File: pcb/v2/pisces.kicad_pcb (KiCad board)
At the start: 2 copper layers, 137.8 x 60.1 mm, 61 parts, among them J1 USB_B_Micro, J2 AudioJack4, SW1 SW_PUSH, SW10 SW_PUSH, SW11 SW_PUSH, SW12 SW_PUSH, SW13 SW_PUSH, SW14 SW_PUSH, SW15 SW_PUSH, SW16 SW_PUSH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

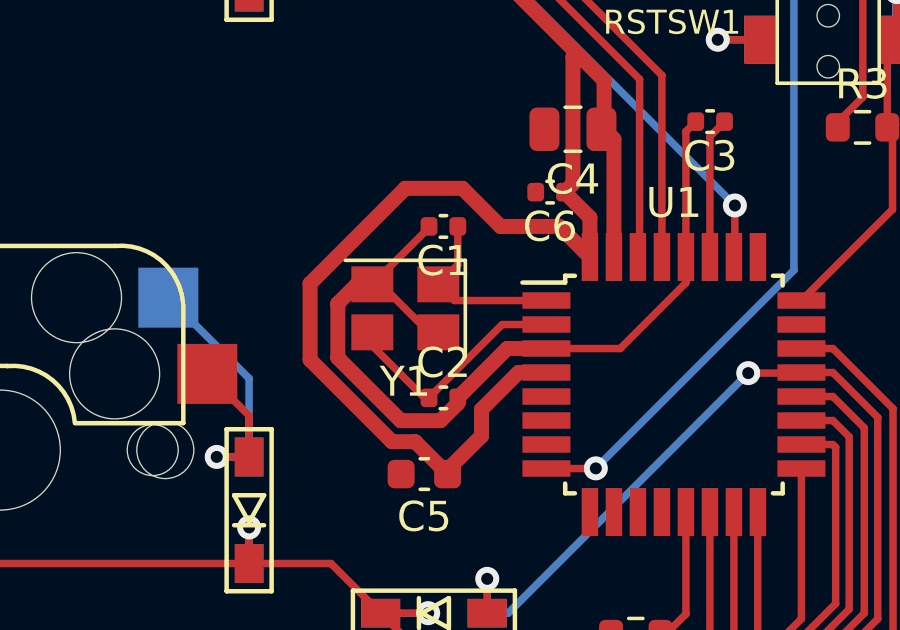
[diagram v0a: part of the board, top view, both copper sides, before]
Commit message: Removed external link to footprint library (#33)
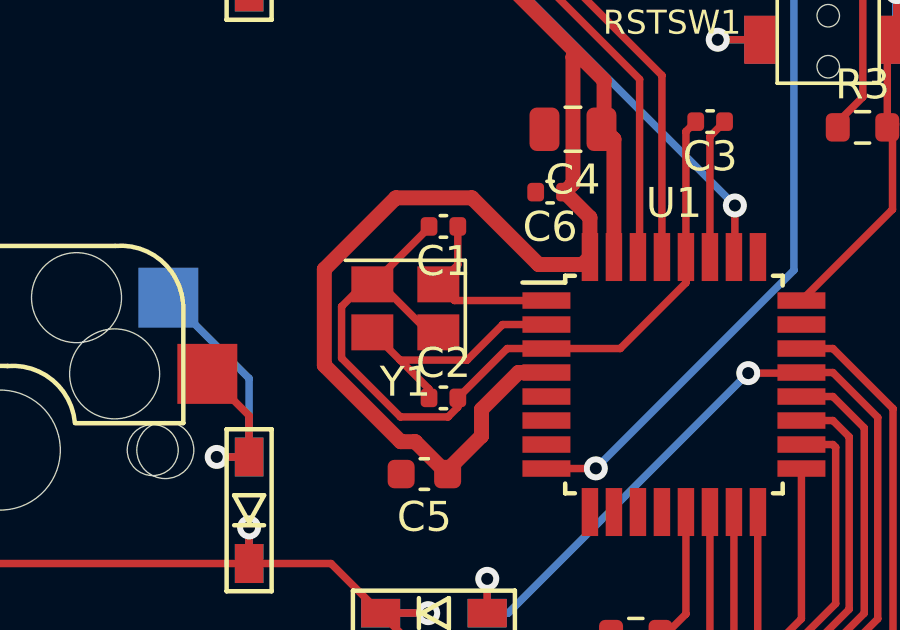
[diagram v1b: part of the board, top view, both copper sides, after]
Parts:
- D1, D10, D11, D12, D13, D14, D15, D16, D17, D18, D19, D2, D3, D4, D5, D6, D7, D8, D9, D_H1: footprint kbd:D3_SMD -> pisces_v2:D3_SMD
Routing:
- net VCC: track 75.2 -> 74.6 mm

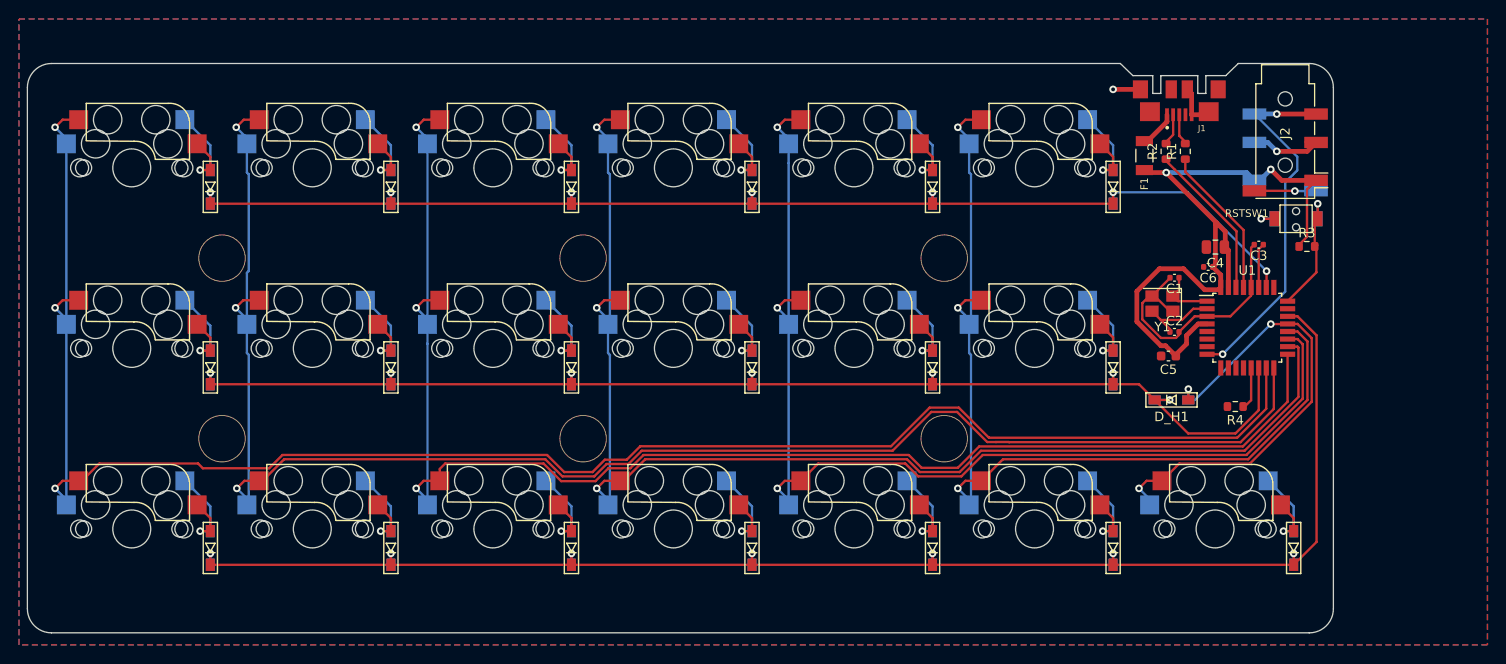
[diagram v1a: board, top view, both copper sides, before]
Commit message: KiCad Updated to 6.0.7 (#34)
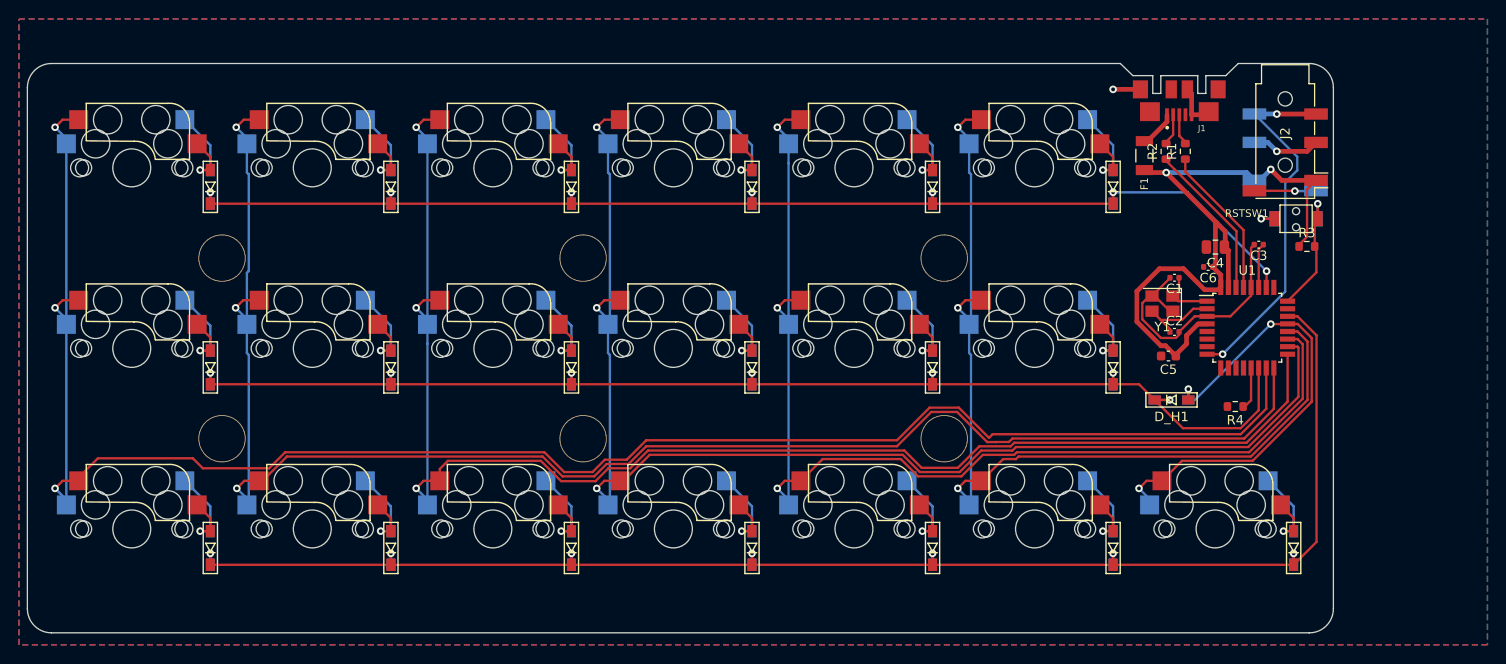
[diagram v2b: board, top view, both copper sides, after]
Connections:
- J1 pad 4: Net-(J1-Pad4) -> unconnected-(J1-Pad4)
- J2 pad S: Net-(J2-PadS) -> unconnected-(J2-PadS)
- U1 pad 10: Net-(U1-Pad10) -> unconnected-(U1-Pad10)
- U1 pad 11: Net-(U1-Pad11) -> unconnected-(U1-Pad11)
- U1 pad 12: Net-(U1-Pad12) -> unconnected-(U1-Pad12)
- U1 pad 23: Net-(U1-Pad23) -> unconnected-(U1-Pad23)
- U1 pad 25: Net-(U1-Pad25) -> unconnected-(U1-Pad25)
- U1 pad 5: Net-(U1-Pad5) -> unconnected-(U1-Pad5)
- U1 pad 6: Net-(U1-Pad6) -> unconnected-(U1-Pad6)
- U1 pad 7: Net-(U1-Pad7) -> unconnected-(U1-Pad7)
- U1 pad 9: Net-(U1-Pad9) -> unconnected-(U1-Pad9)
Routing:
- net Net-(J2-PadS): track 6.67 -> 0.00 mm, vias 1 -> 0
- net unconnected-(J2-PadS): track 0.00 -> 6.53 mm, vias 0 -> 1
- net col0: track 190.8 -> 191.5 mm
- net col2: track 154.6 -> 155.2 mm
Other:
- net class Default removed

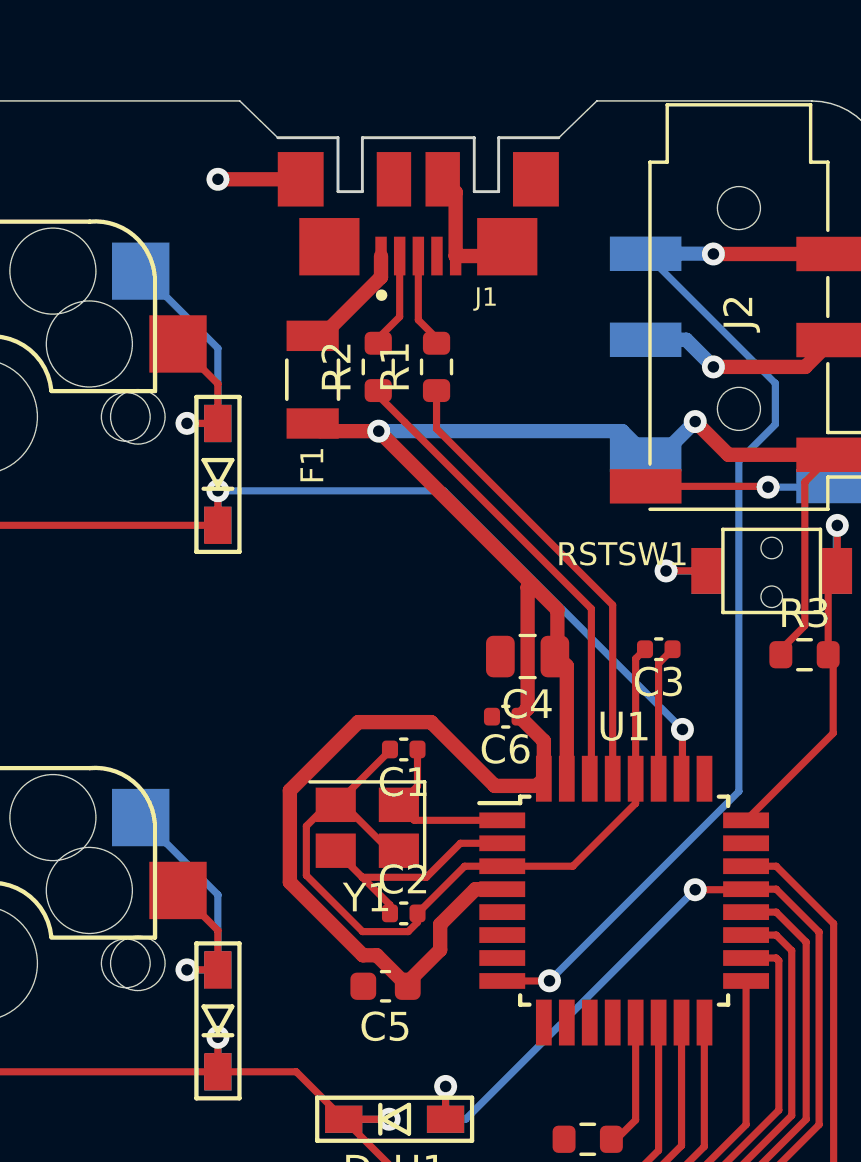
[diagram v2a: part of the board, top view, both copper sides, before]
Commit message: Updated KiCad 7.0.10 (#35)
* Removed ERC errors as many as possible

* symbols も外部依存をなくした
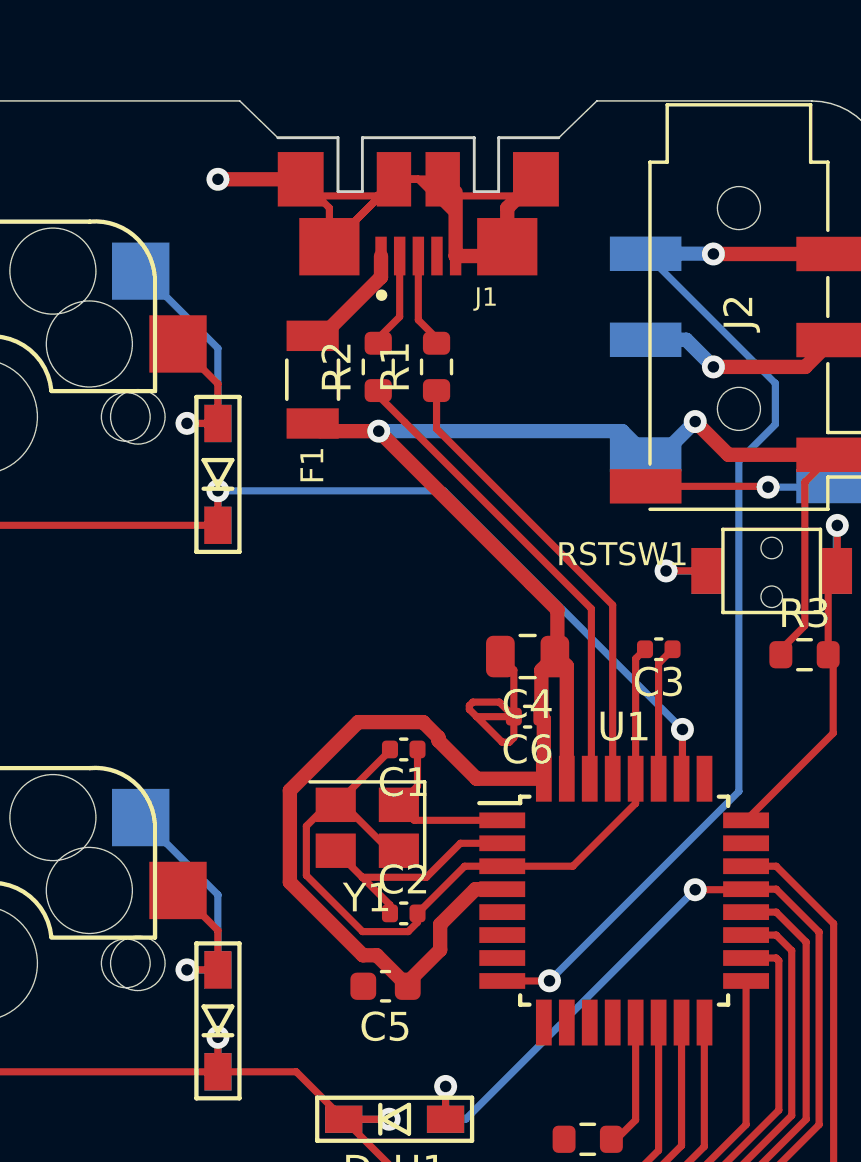
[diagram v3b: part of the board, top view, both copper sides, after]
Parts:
- HOLE1, HOLE13, HOLE14, HOLE2, HOLE7, HOLE8: footprint kbd:HOLE -> pisces_v2:HOLE
- moved C6 0.76 mm to (164.3, 60.5)
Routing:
- net GND: track 46.8 -> 82.0 mm
- net VCC: track 74.4 -> 71.4 mm
